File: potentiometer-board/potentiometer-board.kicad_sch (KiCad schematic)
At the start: 6 parts, among them J1 Conn_01x03

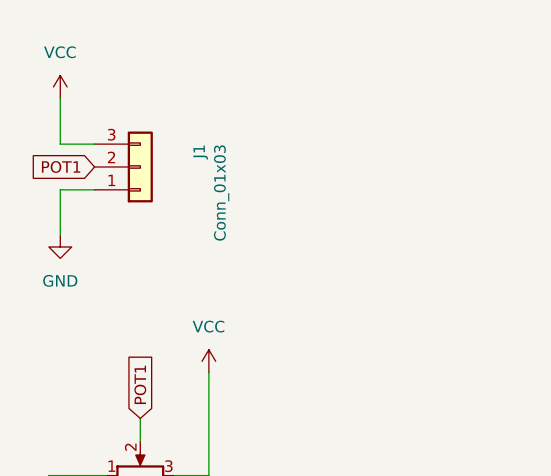
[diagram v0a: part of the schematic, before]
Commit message: Update all boards to KiCad 9.0 (#44)
* update dimmer board to KiCad version 9

* update dual encoder board to KiCad version 9

* update input shifter board, start numbering with zero instead one

* update MAX7219 breakout board to KiCad version 9

* add 3 pol JST connector

* updatge template to KiCad version 9

* update potentiometer board to KiCad version 9, use JST connector from MF lib

* update 6pin JST connector

* update prototyping board to KiCad version 9

* update symbols on dimmer board, fixed DRC

* update symbols from MAX7219 breakout board

* add Screw Terminalblocks to footprint lib and 3D models

* use screw terminals from MF lib

* fixed outline of Potentiometer board

* fixed missing IDC footprints error

* add MAX7219 symbol

* use MAX7219 symbol from MF lib

* add Mega2560mini symbol and footprint to MF library

* use Mega2560mini symbol and footprint from MF library

* add used Dual Encoder symbol and footprint to MF lib

* use footprint and symbol for Dual Encoder from MF lib
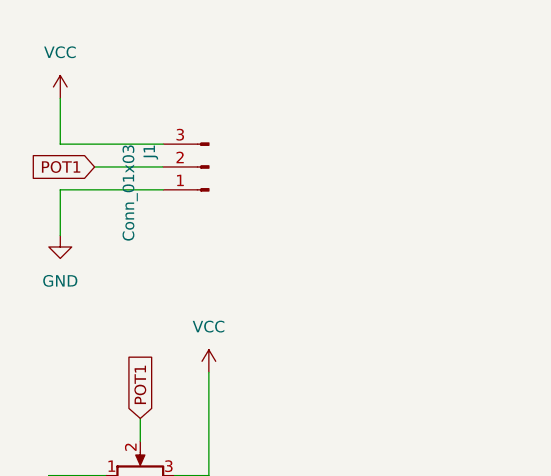
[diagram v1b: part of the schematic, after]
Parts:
- J1: symbol Connector_Generic:Conn_01x03 -> mobiflight-library:JST-XH_03_Pin_vertical
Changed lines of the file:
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@@
 (kicad_sch
-	(version 20231120)
+	(version 20250114)
 	(generator "eeschema")
-	(generator_version "8.0")
+	(generator_version "9.0")
 	(paper "A4")
 	(wire
 		(pts
+			(xy 44.45 35.56) (xy 36.83 35.56)
+		)
+		(stroke
+			(width 0)
+			(type default)
+		)
+	)
+	(wire
+		(pts
 			(xy 41.91 63.5) (xy 41.91 66.04)
 		)
@@
 	(wire
 		(pts
-			(xy 33.02 33.02) (xy 36.83 33.02)
+			(xy 33.02 33.02) (xy 44.45 33.02)
 		)
 		(stroke
@@
 	(wire
 		(pts
-			(xy 36.83 38.1) (xy 33.02 38.1)
+			(xy 44.45 38.1) (xy 33.02 38.1)
 		)
 		(stroke
@@
 			)
 		)
-		(property "Description" ""
+		(property "Description" "Mounting Hole with connection"
 			(at 118.11 38.1 0)
 			(effects
@@
 			)
 		)
-		(property "Description" ""
+		(property "Description" "Mounting Hole with connection"
 			(at 118.11 30.48 0)
 			(effects
@@
 	)
 	(symbol
-		(lib_id "Connector_Generic:Conn_01x03")
-		(at 41.91 35.56 0)
-		(mirror x)
+		(lib_id "mobiflight-library:JST-XH_03_Pin_vertical")
+		(at 49.53 35.56 180)
 		(unit 1)
 		(exclude_from_sim no)
@@
 		(dnp no)
 		(property "Reference" "J1"
-			(at 48.4886 33.02 90)
+			(at 42.9514 33.02 90)
 			(effects
 				(font
@@
 		)
 		(property "Value" "Conn_01x03"
-			(at 50.8 33.02 90)
+			(at 40.64 33.02 90)
 			(effects
 				(font
@@
 		)
 		(property "Footprint" "Connector_JST:JST_XH_B3B-XH-A_1x03_P2.50mm_Vertical"
-			(at 41.91 35.56 0)
+			(at 49.53 35.56 0)
 			(effects
 				(font
@@
 		)
 		(property "Datasheet" "~"
-			(at 41.91 35.56 0)
-			(effects
-				(font
-					(size 1.27 1.27)
-				)
-				(hide yes)
-			)
-		)
-		(property "Description" ""
-			(at 41.91 35.56 0)
+			(at 49.53 35.56 0)
+			(effects
+				(font
+					(size 1.27 1.27)
+				)
+				(hide yes)
+			)
+		)
+		(property "Description" "Generic connector, single row, 01x03, script generated"
+			(at 49.53 35.56 0)
 			(effects
 				(font
@@
 		)
 		(property "LCSC" "C144394"
-			(at 41.91 35.56 0)
+			(at 49.53 35.56 0)
 			(effects
 				(font
@@
 			)
 		)
-		(property "Description" ""
+		(property "Description" "Mounting Hole with connection"
 			(at 118.11 22.86 0)
 			(effects
@@
 			)
 		)
-		(property "Description" ""
+		(property "Description" "Power symbol creates a global label with name \"GND\" , ground"
 			(at 31.75 76.2 0)
 			(effects
@@
 			)
 		)
-		(property "Description" ""
+		(property "Description" "Mounting Hole with connection"
 			(at 118.11 45.72 0)
 			(effects
@@
 			)
 		)
-		(property "Description" ""
+		(property "Description" "Power symbol creates a global label with name \"GND\" , ground"
 			(at 33.02 43.18 0)
 			(effects
@@
 		)
 	)
+	(embedded_fonts no)
 )
